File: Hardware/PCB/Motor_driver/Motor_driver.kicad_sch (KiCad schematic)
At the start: 85 parts, among them IC1 A89307KETSR-J, J1 Conn_01x02, J2 Conn_01x05, J3 Conn_01x03, J4 Conn_ST_STDC14, J5 USB_C_Receptacle_USB2.0_16P, J6 USB_C_Receptacle_USB2.0_16P, SW1 SW_Push, SW2 SW_Push, SW3 SW_DIP_x02, SW4 SW_Push, SW5 SW_Push, SW6 SW_Push, U1 AZ1117-3.3, U3 STM32L412KBTx, U4 USBLC6-2SC6

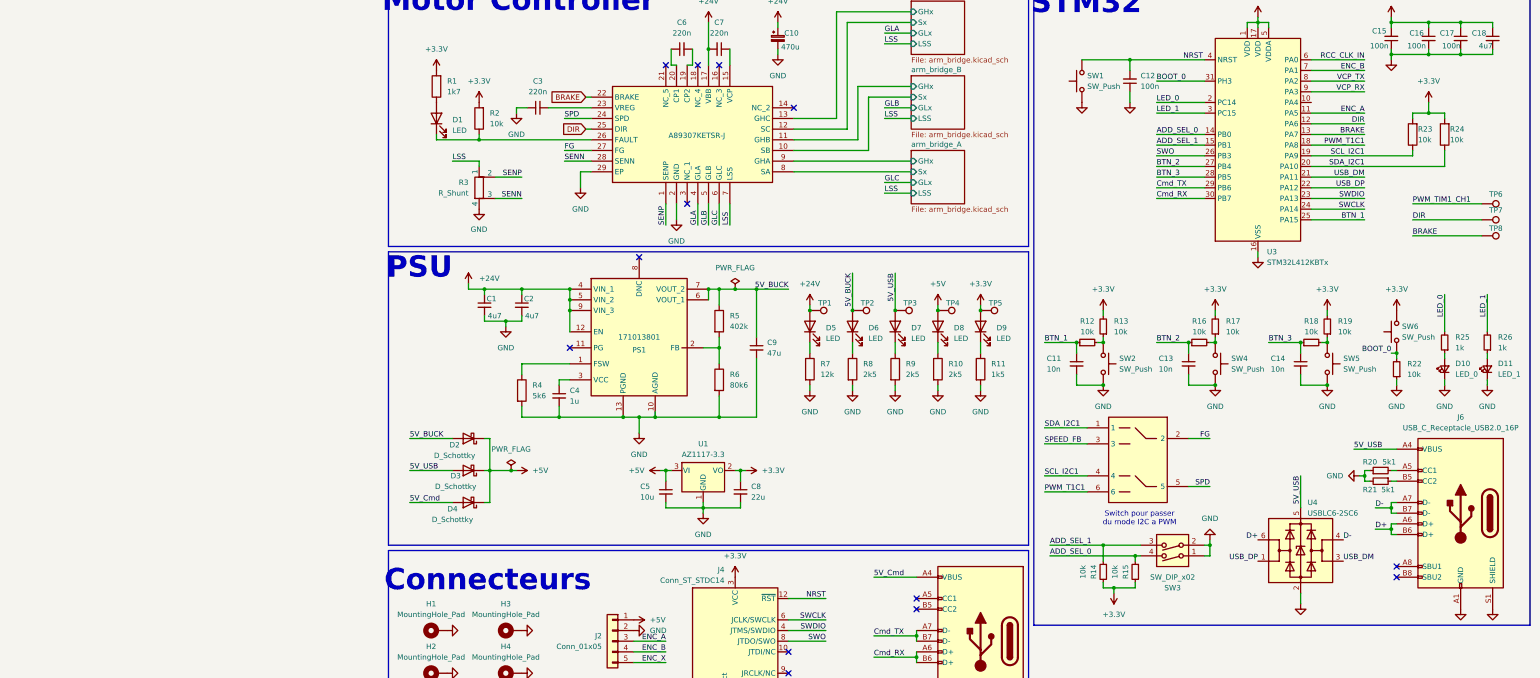
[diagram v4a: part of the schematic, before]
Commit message: Pcb moteur routé
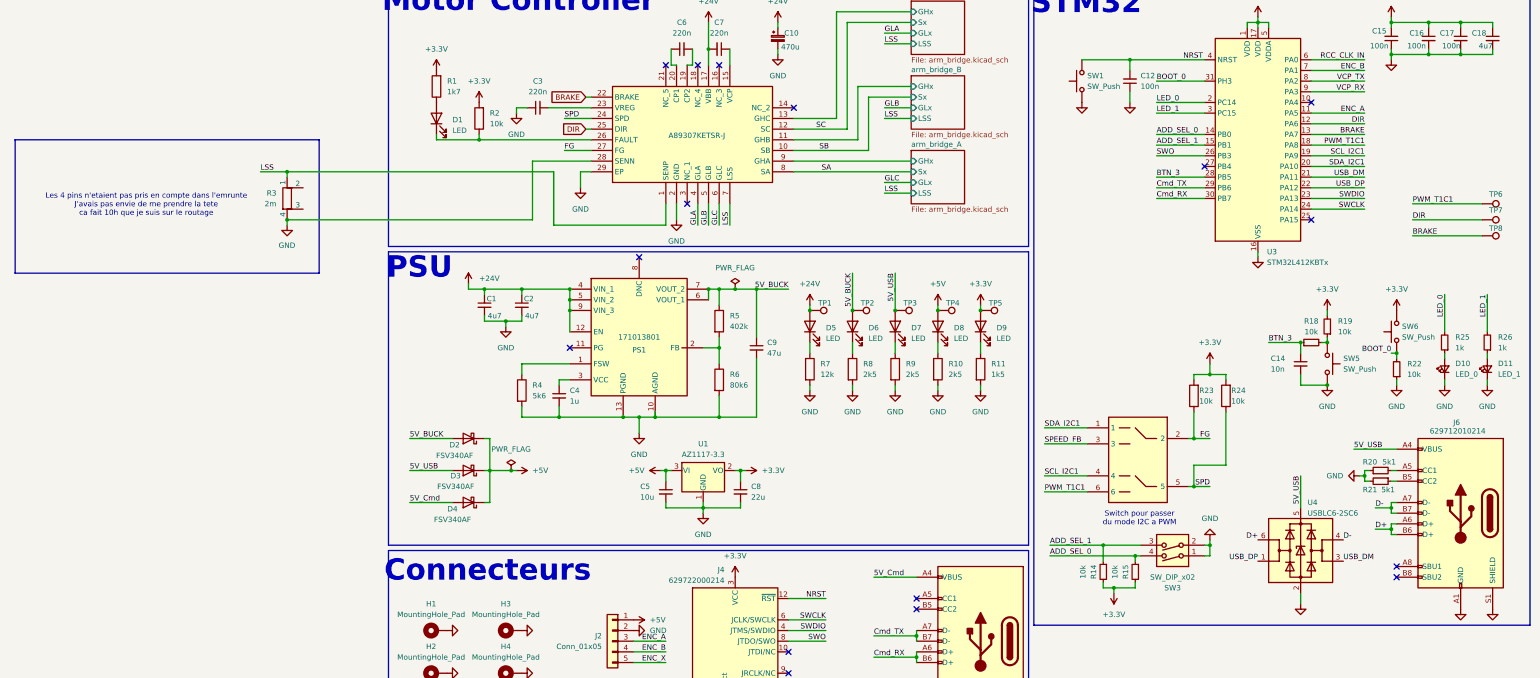
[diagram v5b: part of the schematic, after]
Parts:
- removed C11, C13: 10n, Capacitor_SMD:C_0402_1005Metric, symbol Device:C_Small
- removed R12, R13, R16, R17: 10k, Resistor_SMD:R_0402_1005Metric, symbol Device:R_Small
- removed SW2, SW4: SW_Push, symbol Switch:SW_Push
- C10: footprint (none) -> SamacSys_Parts:CAPAE1710X1700N
- D2, D3, D4: value D_Schottky -> FSV340AF; footprint (none) -> Diode_SMD:D_SMA
- J1: footprint (none) -> Connector_AMASS:AMASS_XT60PW-M_1x02_P7.20mm_Horizontal
- J2: footprint (none) -> Connector_JST:JST_XH_B5B-XH-A_1x05_P2.50mm_Vertical
- J3: footprint (none) -> Connector_Phoenix_GMSTB:PhoenixContact_GMSTBVA_2,5_3-G-7,62_1x03_P7.62mm_Vertical
- J4: value Conn_ST_STDC14 -> 629722000214
- J5: footprint (none) -> Connector_USB:USB_C_Receptacle_HCTL_HC-TYPE-C-16P-01A
- J6: value USB_C_Receptacle_USB2.0_16P -> 629712010214; footprint (none) -> Connector_USB:USB_C_Receptacle_GCT_USB4115-03-C
- R3: value R_Shunt -> 2m; footprint (none) -> Resistor_SMD:R_2512_6332Metric
- SW1, SW5, SW6: footprint (none) -> SamacSys_Parts:430152043826
- SW3: footprint (none) -> SamacSys_Parts:418121270802
- U1: footprint (none) -> Package_TO_SOT_SMD:SOT-223
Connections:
- net PWM_TIM1_CH1 is gone; now on net PWM_T1C1: TP6.1
- net arm_bridge_A/Sx is gone; now on net SA: IC1.8 (SA)
- net arm_bridge_B/Sx is gone; now on net SB: IC1.10 (SB)
- net arm_bridge_C/Sx is gone; now on net SC: IC1.12 (SC)
- net +3.3V: now also U1.4 (VO)
- net FG: now also R23.1
- net GND: now also IC1.28 (SENN)
- net LSS: now also IC1.1 (SENP)
- net SCL_I2C1: no longer R23.1
- net SDA_I2C1: no longer R24.1
- net SPD: now also R24.1
- net BTN_1: no longer names the net of U3.25 (PA15)
- net BTN_2: no longer names the net of U3.27 (PB4)
- net SENN: no longer names the net of R3.3
- net SENN: no longer IC1.28 (SENN)
- net SENP: no longer names the net of R3.2
- net SENP: no longer IC1.1 (SENP)
- no-connect marks 15 -> 18
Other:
- note added: "Les 4 pins n'etaient pas pris en compte dans l'emrunte J'avais pas envie de me prendre la tete ca fait 10h que je suis sur le routage"
- moved on the sheet: R23, R24, R3

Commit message: Gerber
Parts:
- R3: footprint Resistor_SMD:R_2512_6332Metric -> Resistor_SMD:R_Shunt_Ohmite_LVK24
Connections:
- net GND: no longer IC1.28 (SENN)
- net LSS: no longer IC1.1 (SENP)
- net at R3.2: now also IC1.1 (SENP)
- net at R3.3: now also IC1.28 (SENN)
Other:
- moved on the sheet: R3
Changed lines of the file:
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@@
 	)
 	(junction
-		(at -11.43 57.15)
-		(diameter 0)
-		(color 0 0 0 0)
-	)
-	(junction
 		(at 143.51 90.17)
 		(diameter 0)
@@
 	)
 	(junction
-		(at -11.43 68.58)
-		(diameter 0)
-		(color 0 0 0 0)
-	)
-	(junction
 		(at 36.83 128.27)
 		(diameter 0)
@@
 	(wire
 		(pts
+			(xy 38.1 60.96) (xy 52.07 60.96)
+		)
+		(stroke
+			(width 0)
+			(type default)
+		)
+	)
+	(wire
+		(pts
 			(xy 232.41 38.1) (xy 245.11 38.1)
 		)
@@
 	(wire
 		(pts
+			(xy 43.18 54.61) (xy 43.18 66.04)
+		)
+		(stroke
+			(width 0)
+			(type default)
+		)
+	)
+	(wire
+		(pts
 			(xy 107.95 166.37) (xy 116.84 166.37)
 		)
@@
 	(wire
 		(pts
-			(xy 78.74 69.85) (xy 52.0433 69.85)
+			(xy 78.74 69.85) (xy 52.07 69.85)
 		)
 		(stroke
@@
 	(wire
 		(pts
-			(xy -17.78 57.15) (xy -11.43 57.15)
+			(xy 27.94 57.15) (xy 34.29 57.15)
 		)
 		(stroke
@@
 	(wire
 		(pts
-			(xy -11.43 57.15) (xy 52.0433 57.15)
-		)
-		(stroke
-			(width 0)
-			(type default)
-		)
-	)
-	(wire
-		(pts
 			(xy 251.46 140.97) (xy 251.46 142.24)
 		)
@@
 	(wire
 		(pts
-			(xy 46.99 54.61) (xy 60.96 54.61)
-		)
-		(stroke
-			(width 0)
-			(type default)
-		)
-	)
-	(wire
-		(pts
 			(xy 78.74 130.81) (xy 78.74 128.27)
 		)
@@
 	(wire
 		(pts
-			(xy 52.0433 69.85) (xy 52.0433 57.15)
+			(xy 52.07 69.85) (xy 52.07 60.96)
 		)
 		(stroke
@@
 	(wire
 		(pts
+			(xy 43.18 54.61) (xy 60.96 54.61)
+		)
+		(stroke
+			(width 0)
+			(type default)
+		)
+	)
+	(wire
+		(pts
 			(xy 229.87 100.33) (xy 229.87 97.79)
 		)
@@
 	(wire
 		(pts
-			(xy -11.43 58.42) (xy -11.43 57.15)
+			(xy 34.29 58.42) (xy 34.29 57.15)
 		)
 		(stroke
@@
 	(wire
 		(pts
+			(xy 43.18 66.04) (xy 38.1 66.04)
+		)
+		(stroke
+			(width 0)
+			(type default)
+		)
+	)
+	(wire
+		(pts
 			(xy 208.28 148.59) (xy 208.28 146.05)
 		)
@@
 	(wire
 		(pts
-			(xy 46.99 68.58) (xy 46.99 54.61)
-		)
-		(stroke
-			(width 0)
-			(type default)
-		)
-	)
-	(wire
-		(pts
 			(xy 143.51 88.9) (xy 143.51 90.17)
 		)
@@
 	(wire
 		(pts
-			(xy -11.43 68.58) (xy 46.99 68.58)
-		)
-		(stroke
-			(width 0)
-			(type default)
-		)
-	)
-	(wire
-		(pts
 			(xy 177.8 30.48) (xy 189.23 30.48)
 		)
@@
 	(wire
 		(pts
-			(xy -11.43 69.85) (xy -11.43 68.58)
+			(xy 34.29 69.85) (xy 34.29 68.58)
 		)
 		(stroke
@@
 	)
 	(label "LSS"
-		(at -17.78 57.15 0)
+		(at 27.94 57.15 0)
 		(effects
 			(font
@@
 	(symbol
 		(lib_id "Device:R_Shunt")
-		(at -11.43 63.5 0)
+		(at 34.29 63.5 0)
 		(unit 1)
 		(exclude_from_sim no)
@@
 		(fields_autoplaced yes)
 		(property "Reference" "R3"
-			(at -13.97 62.2299 0)
+			(at 31.75 62.2299 0)
 			(effects
 				(font
@@
 		)
 		(property "Value" "2m"
-			(at -13.97 64.7699 0)
+			(at 31.75 64.7699 0)
 			(effects
 				(font
@@
 			)
 		)
-		(property "Footprint" "Resistor_SMD:R_2512_6332Metric"
-			(at -13.208 63.5 90)
+		(property "Footprint" "Resistor_SMD:R_Shunt_Ohmite_LVK24"
+			(at 32.512 63.5 90)
 			(effects
 				(font
@@
 		)
 		(property "Datasheet" "~"
-			(at -11.43 63.5 0)
+			(at 34.29 63.5 0)
 			(effects
 				(font
@@
 		)
 		(property "Description" "Shunt resistor"
-			(at -11.43 63.5 0)
+			(at 34.29 63.5 0)
 			(effects
 				(font
@@
 	(symbol
 		(lib_id "power:GND")
-		(at -11.43 69.85 0)
+		(at 34.29 69.85 0)
 		(unit 1)
 		(exclude_from_sim no)
@@
 		(dnp no)
 		(property "Reference" "#PWR06"
-			(at -11.43 76.2 0)
+			(at 34.29 76.2 0)
 			(effects
 				(font
@@
 		)
 		(property "Value" "GND"
-			(at -13.462 74.676 0)
+			(at 32.258 74.676 0)
 			(effects
 				(font
@@
 		)
 		(property "Footprint" ""
-			(at -11.43 69.85 0)
+			(at 34.29 69.85 0)
 			(effects
 				(font
@@
 		)
 		(property "Datasheet" ""
-			(at -11.43 69.85 0)
+			(at 34.29 69.85 0)
 			(effects
 				(font
@@
 		)
 		(property "Description" "Power symbol creates a global label with name \"GND\" , ground"
-			(at -11.43 69.85 0)
+			(at 34.29 69.85 0)
 			(effects
 				(font
